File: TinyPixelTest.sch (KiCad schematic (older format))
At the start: 40 parts, among them IC1 ATTINY2313-S, P1 CONN_01X04, P2 CONN_01X04, P3 CONN_01X04, P4 CONN_01X04

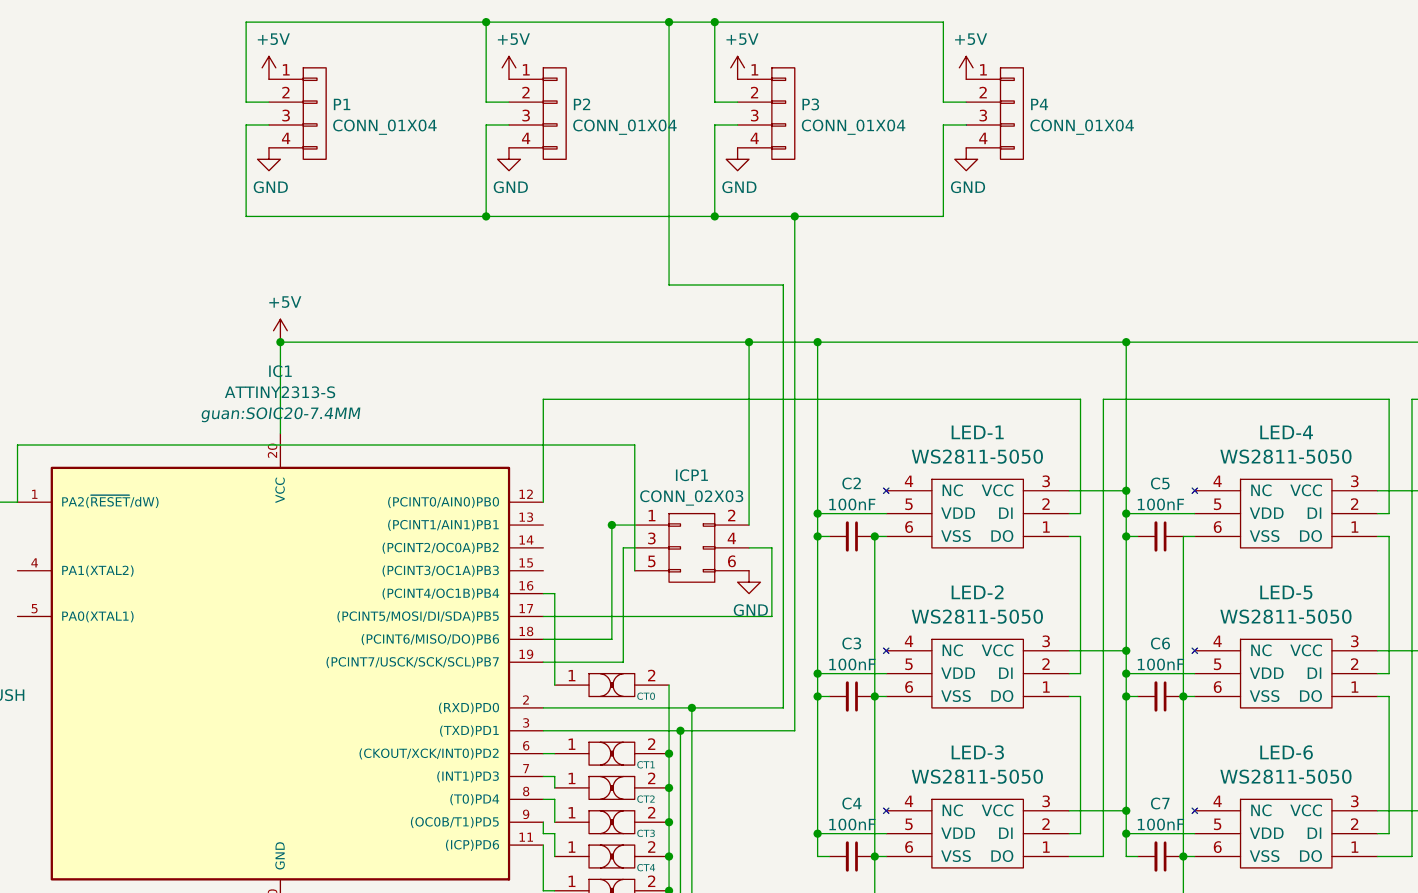
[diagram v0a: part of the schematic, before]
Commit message: Switched from 4 pin to 7 pin symmetrical connectors
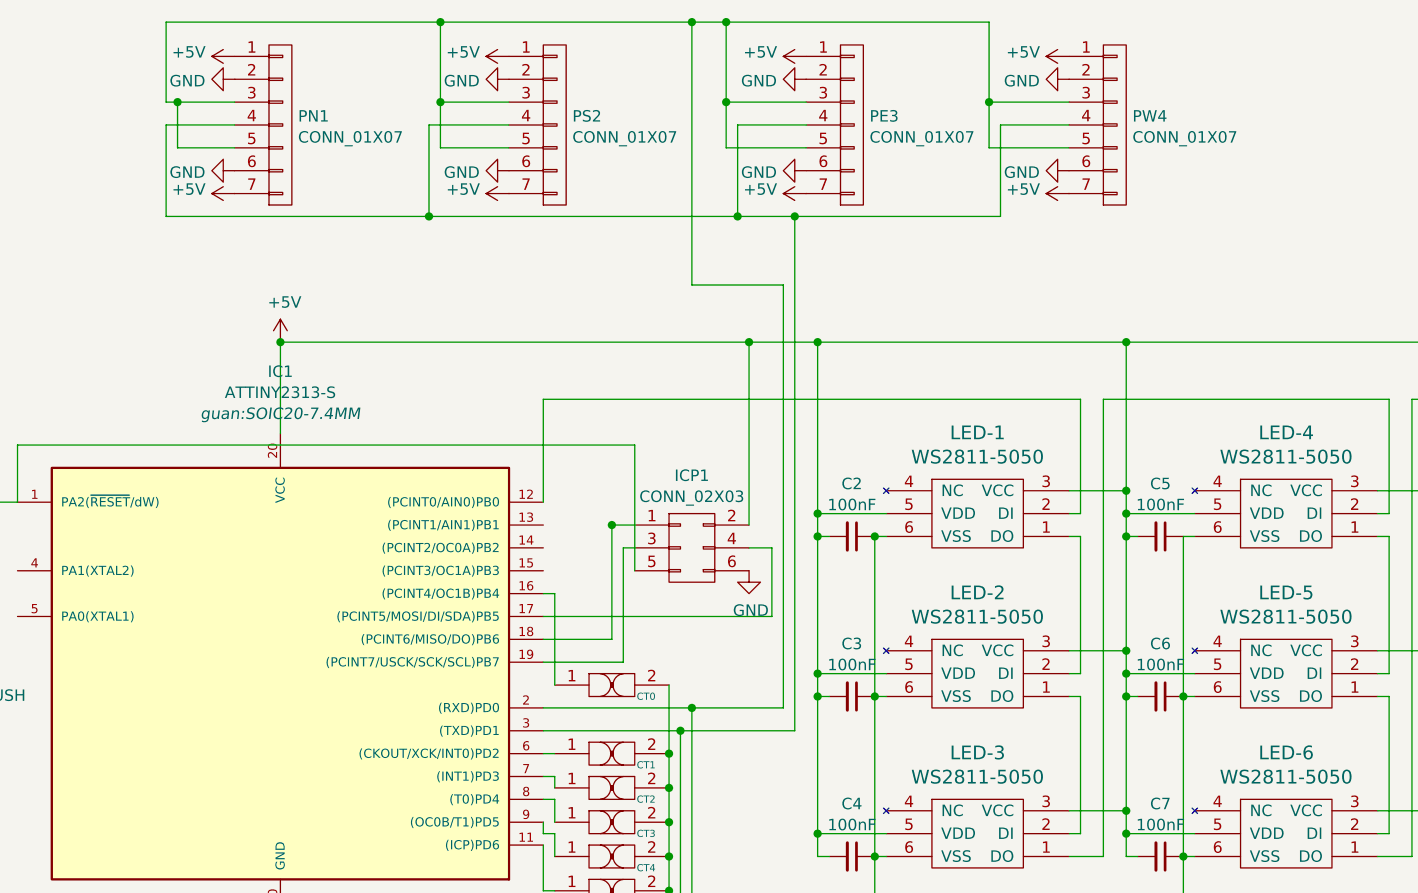
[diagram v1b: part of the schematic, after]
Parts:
- removed P1, P2, P3, P4: CONN_01X04, Pin_Headers:Pin_Header_Angled_1x04, symbol CONN_01X04
- added PE3, PN1: CONN_01X07, Pin_Headers:Pin_Header_Angled_1x07, symbol CONN_01X07
- added PS2, PW4: CONN_01X07, Socket_Strips:Socket_Strip_Angled_1x07, symbol CONN_01X07
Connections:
- net +5V: now also PE3.1 (P1), PE3.7 (P7), PN1.1 (P1), PN1.7 (P7), PS2.1 (P1), PS2.7 (P7), PW4.1 (P1), PW4.7 (P7)
- net GND: now also PE3.2 (P2), PE3.6 (P6), PN1.2 (P2), PN1.6 (P6), PS2.2 (P2), PS2.6 (P6), PW4.2 (P2), PW4.6 (P6)
- net at ESP1.2 (P2), IC1.2 ((RXD)PD0): now also PE3.3 (P3), PE3.5 (P5), PN1.3 (P3), PN1.5 (P5), PS2.3 (P3), PS2.5 (P5), PW4.3 (P3), PW4.5 (P5)
- net at ESP1.4 (P4), IC1.3 ((TXD)PD1): now also PE3.4 (P4), PN1.4 (P4), PS2.4 (P4), PW4.4 (P4)

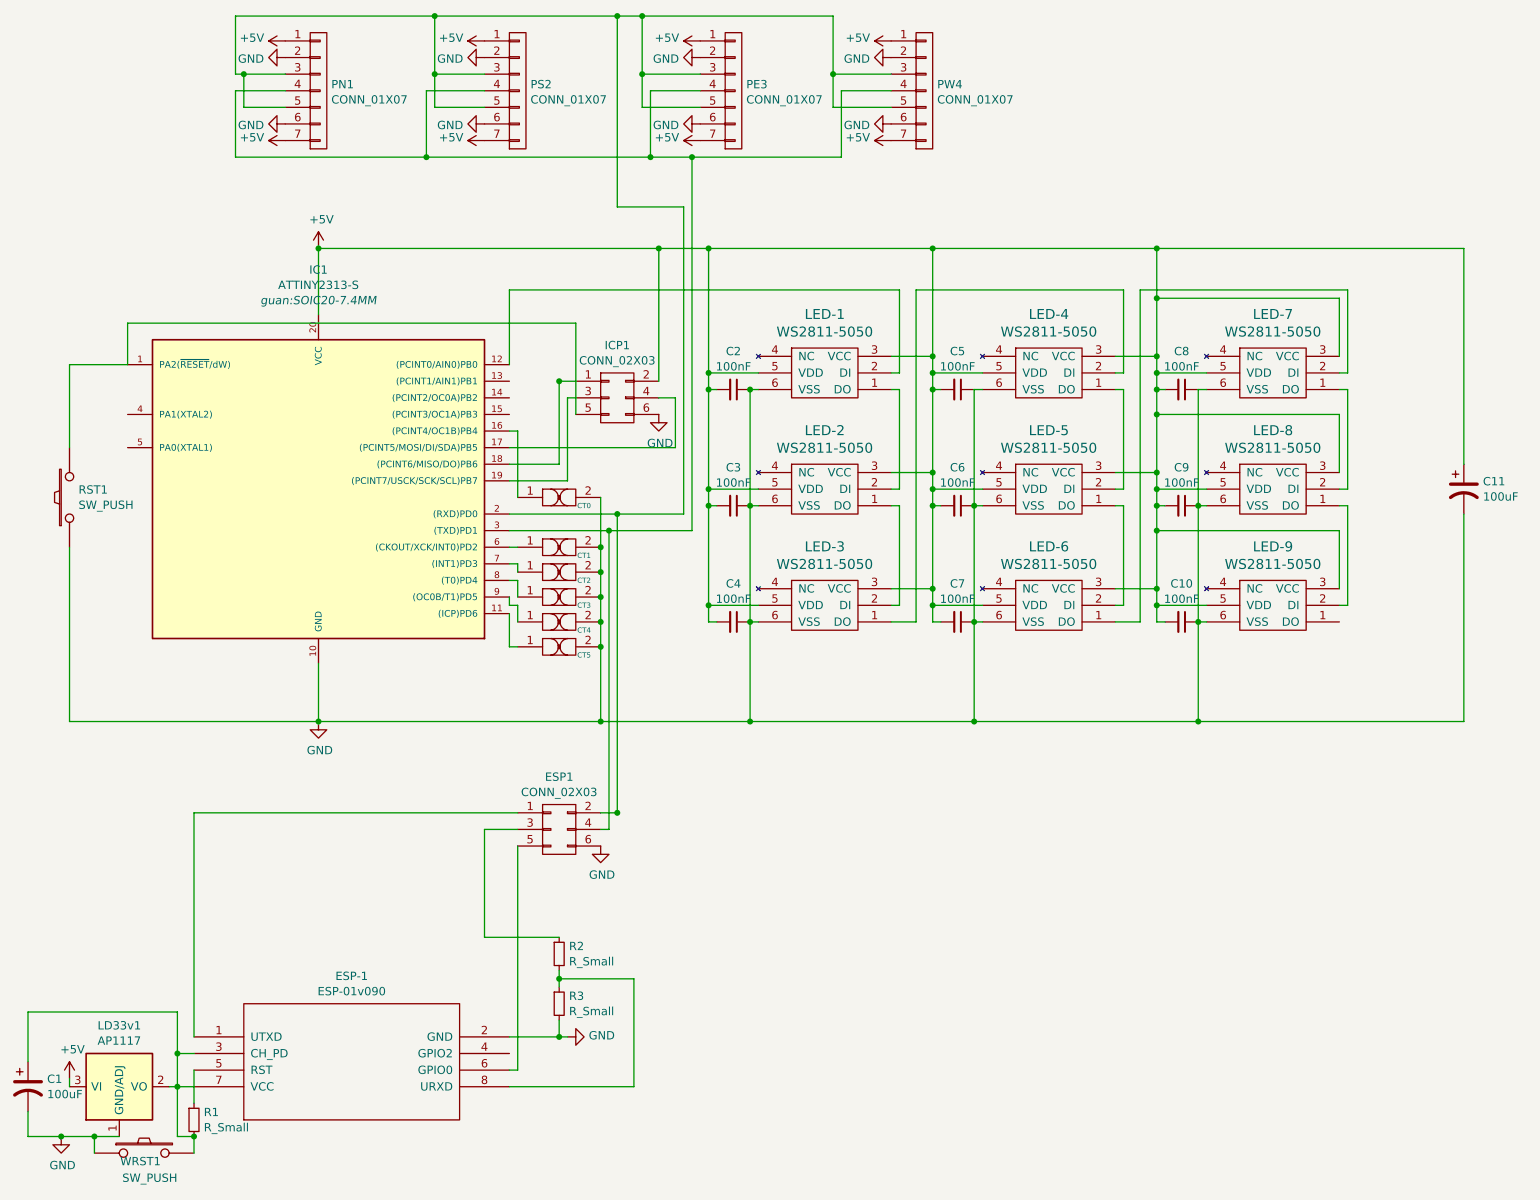
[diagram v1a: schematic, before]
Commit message: Fixed wire position
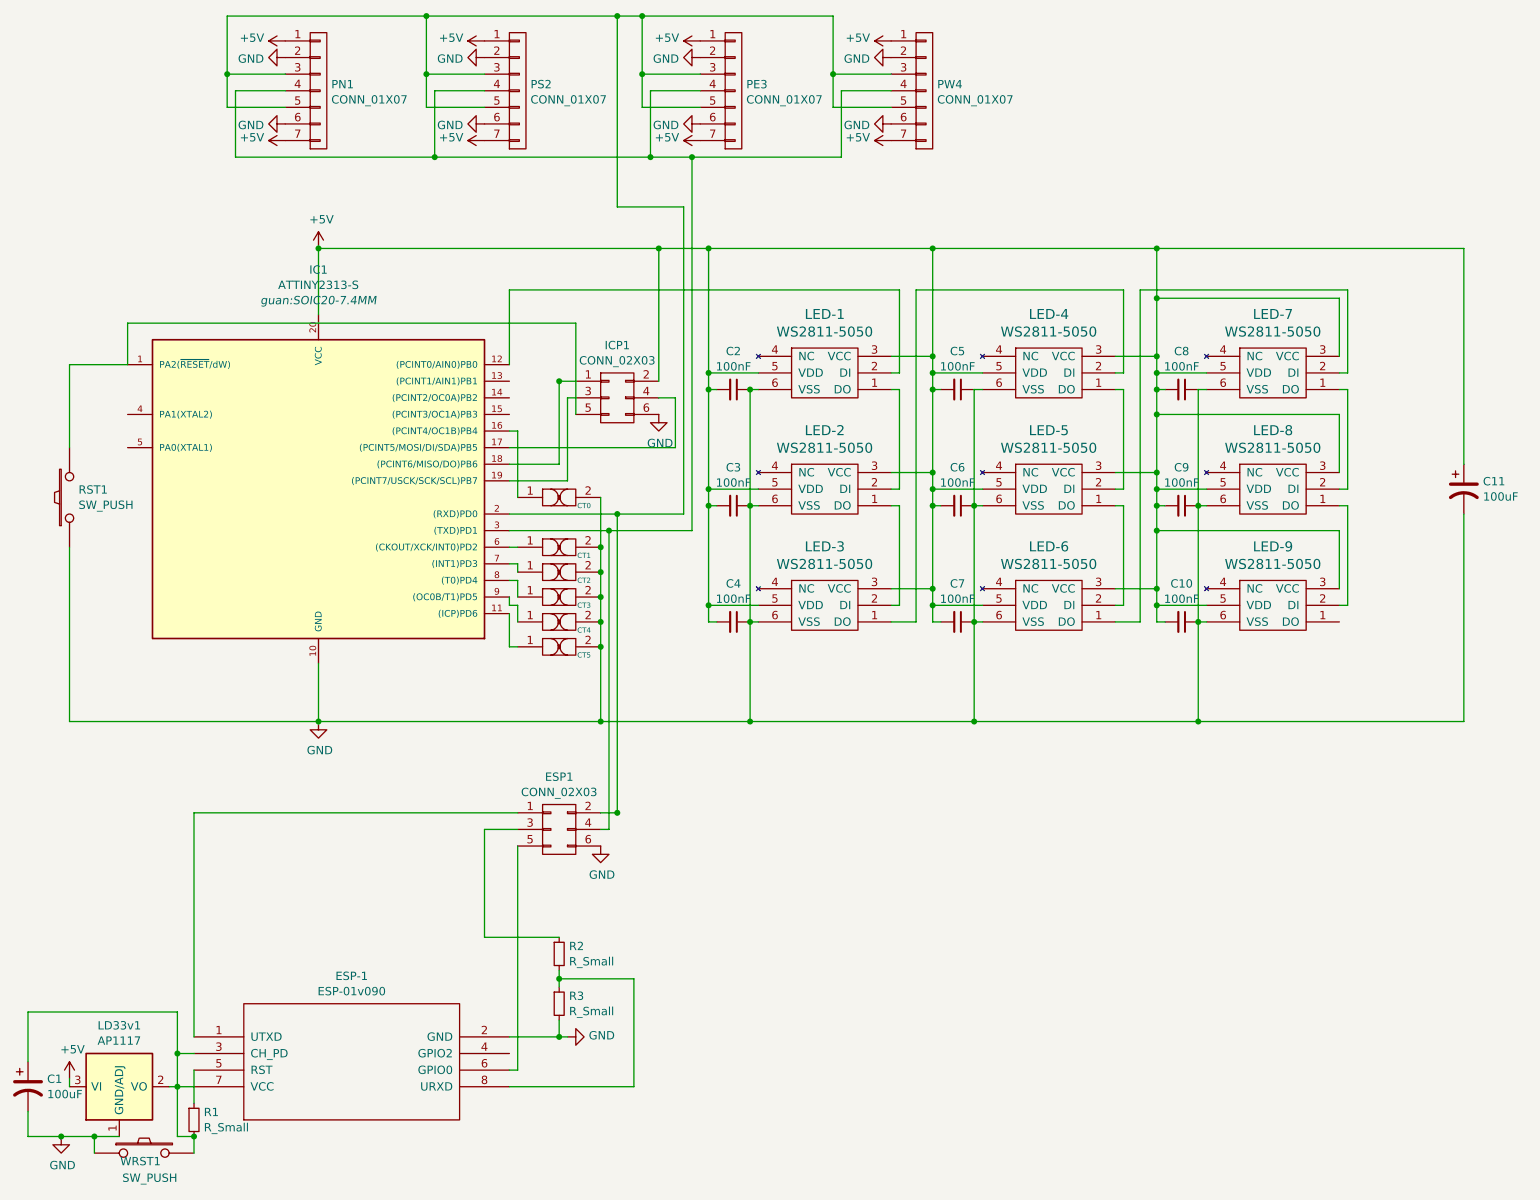
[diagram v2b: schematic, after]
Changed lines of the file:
@@
 $EndComp
 Wire Wire Line
-	4750 1950 4750 4200
+	4750 1950 4750 2700
+Wire Wire Line
+	4750 2700 4750 2800
+Wire Wire Line
+	4750 2800 4750 3400
+Wire Wire Line
+	4750 3400 4750 3500
+Wire Wire Line
+	4750 3500 4750 4100
+Wire Wire Line
+	4750 4100 4750 4200
 Wire Wire Line
 	4750 4100 5050 4100
@@
 Connection ~ 4750 2700
 Wire Wire Line
-	6100 1950 6100 4200
+	6100 1950 6100 2600
+Wire Wire Line
+	6100 2600 6100 2700
+Wire Wire Line
+	6100 2700 6100 2800
+Wire Wire Line
+	6100 2800 6100 3300
+Wire Wire Line
+	6100 3300 6100 3400
+Wire Wire Line
+	6100 3400 6100 3500
+Wire Wire Line
+	6100 3500 6100 4000
+Wire Wire Line
+	6100 4000 6100 4100
+Wire Wire Line
+	6100 4100 6100 4200
 Wire Wire Line
 	6100 4100 6400 4100
@@
 Connection ~ 6100 3400
 Wire Wire Line
-	7450 1950 7450 4200
+	7450 1950 7450 2250
+Wire Wire Line
+	7450 2250 7450 2600
+Wire Wire Line
+	7450 2600 7450 2700
+Wire Wire Line
+	7450 2700 7450 2800
+Wire Wire Line
+	7450 2800 7450 2950
+Wire Wire Line
+	7450 2950 7450 3300
+Wire Wire Line
+	7450 3300 7450 3400
+Wire Wire Line
+	7450 3400 7450 3500
+Wire Wire Line
+	7450 3500 7450 3650
+Wire Wire Line
+	7450 3650 7450 4000
+Wire Wire Line
+	7450 4000 7450 4100
+Wire Wire Line
+	7450 4100 7450 4200
 Wire Wire Line
 	7450 4100 7750 4100
@@
 Connection ~ 7450 2700
 Wire Wire Line
-	2400 1950 9300 1950
+	2400 1950 4450 1950
+Wire Wire Line
+	4450 1950 4750 1950
+Wire Wire Line
+	4750 1950 6100 1950
+Wire Wire Line
+	6100 1950 7450 1950
+Wire Wire Line
+	7450 1950 9300 1950
 Connection ~ 6100 1950
 Wire Wire Line
 	5000 2800 5050 2800
 Wire Wire Line
-	5000 4800 5000 2800
+	5000 4800 5000 4200
+Wire Wire Line
+	5000 4200 5000 3500
+Wire Wire Line
+	5000 3500 5000 2800
 Wire Wire Line
 	5050 3500 5000 3500
@@
 Connection ~ 5000 4200
 Wire Wire Line
-	6350 4800 6350 2800
+	6350 4800 6350 4200
+Wire Wire Line
+	6350 4200 6350 3500
+Wire Wire Line
+	6350 3500 6350 2800
 Wire Wire Line
 	6350 2800 6400 2800
@@
 Connection ~ 6350 4200
 Wire Wire Line
-	7700 4800 7700 2800
+	7700 4800 7700 4200
+Wire Wire Line
+	7700 4200 7700 3500
+Wire Wire Line
+	7700 3500 7700 2800
 Wire Wire Line
 	7700 2800 7750 2800
@@
 Connection ~ 7700 4200
 Wire Wire Line
-	900  4800 9300 4800
+	900  4800 2400 4800
+Wire Wire Line
+	2400 4800 4100 4800
+Wire Wire Line
+	4100 4800 5000 4800
+Wire Wire Line
+	5000 4800 6350 4800
+Wire Wire Line
+	6350 4800 7700 4800
+Wire Wire Line
+	7700 4800 9300 4800
 Connection ~ 6350 4800
 Wire Wire Line
@@
 	900  7000 900  6950
 Wire Wire Line
-	3550 6700 3900 6700
+	3550 6700 3850 6700
+Wire Wire Line
+	3850 6700 3900 6700
 Wire Wire Line
 	1650 5350 1650 6700
 Wire Wire Line
-	3550 3550 4600 3550
-Wire Wire Line
-	650  7300 1200 7300
+	3550 3550 4200 3550
+Wire Wire Line
+	4200 3550 4600 3550
+Wire Wire Line
+	650  7300 850  7300
+Wire Wire Line
+	850  7300 1050 7300
+Wire Wire Line
+	1050 7300 1200 7300
 Wire Wire Line
 	1650 5350 3600 5350
@@
 Connection ~ 3850 6700
 Wire Wire Line
-	3850 6300 3850 6400
+	3850 6300 3850 6350
+Wire Wire Line
+	3850 6350 3850 6400
 Wire Wire Line
 	3850 6350 4300 6350
@@
 Connection ~ 850  7300
 Wire Wire Line
-	1500 7000 1650 7000
+	1500 7000 1550 7000
+Wire Wire Line
+	1550 7000 1650 7000
 Connection ~ 1650 7300
 Wire Wire Line
@@
 	1550 7300 1650 7300
 Wire Wire Line
-	1550 6550 1550 7300
+	1550 6550 1550 6800
+Wire Wire Line
+	1550 6800 1550 7000
+Wire Wire Line
+	1550 7000 1550 7300
 Connection ~ 1550 7000
 Wire Wire Line
@@
 $EndComp
 Wire Wire Line
-	3550 3650 4650 3650
+	3550 3650 4150 3650
+Wire Wire Line
+	4150 3650 4650 3650
 $Comp
 L CUT-1 CT2
@@
 	3550 4350 3600 4350
 Wire Wire Line
-	4100 3450 4100 4800
+	4100 3450 4100 3750
+Wire Wire Line
+	4100 3750 4100 3900
+Wire Wire Line
+	4100 3900 4100 4050
+Wire Wire Line
+	4100 4050 4100 4200
+Wire Wire Line
+	4100 4200 4100 4350
+Wire Wire Line
+	4100 4350 4100 4800
 Connection ~ 4100 4800
 Connection ~ 4100 4350
@@
 	4700 900  4350 900
 Wire Wire Line
-	4350 550  4350 1100
-Wire Wire Line
-	1900 550  5500 550
-Wire Wire Line
-	1900 550  1900 900
-Wire Wire Line
-	1900 900  2200 900
-Wire Wire Line
-	3100 550  3100 1100
-Wire Wire Line
-	3100 900  3400 900
-Connection ~ 3100 550
-Wire Wire Line
-	5500 550  5500 1100
+	4350 550  4350 900
+Wire Wire Line
+	4350 900  4350 1100
+Wire Wire Line
+	1850 550  3050 550
+Wire Wire Line
+	3050 550  4200 550
+Wire Wire Line
+	4200 550  4350 550
+Wire Wire Line
+	4350 550  5500 550
+Wire Wire Line
+	1850 550  1850 900
+Wire Wire Line
+	1850 900  1850 900
+Wire Wire Line
+	1850 900  2200 900
+Wire Wire Line
+	3050 550  3050 900
+Wire Wire Line
+	3050 900  3050 1100
+Wire Wire Line
+	3050 900  3400 900
+Connection ~ 3050 550
+Wire Wire Line
+	5500 550  5500 900
+Wire Wire Line
+	5500 900  5500 1100
 Wire Wire Line
 	5500 900  5850 900
@@
 	5550 1000 5550 1400
 Wire Wire Line
-	5550 1400 1900 1400
+	5550 1400 4650 1400
+Wire Wire Line
+	4650 1400 4400 1400
+Wire Wire Line
+	4400 1400 3100 1400
+Wire Wire Line
+	3100 1400 1900 1400
 Wire Wire Line
 	1900 1400 1900 1000
@@
 	1900 1000 2200 1000
 Wire Wire Line
-	3400 1000 3050 1000
-Wire Wire Line
-	3050 1000 3050 1400
-Connection ~ 3050 1400
+	3400 1000 3100 1000
+Wire Wire Line
+	3100 1000 3100 1400
+Connection ~ 3100 1400
 Wire Wire Line
 	4700 1000 4400 1000
@@
 $EndComp
 Wire Wire Line
-	1950 900  1950 1100
-Wire Wire Line
-	1950 1100 2200 1100
-Connection ~ 1950 900
+	1850 900  1850 1100
+Wire Wire Line
+	1850 1100 2200 1100
+Connection ~ 1850 900
 $Comp
 L CONN_01X07 PS2
@@
 Connection ~ 4350 900
 Wire Wire Line
-	3100 1100 3400 1100
-Connection ~ 3100 900
+	3050 1100 3400 1100
+Connection ~ 3050 900
 $Comp
 L GND #PWR012

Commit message: Uhhh
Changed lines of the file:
@@
 Connection ~ 4150 3650
 Wire Wire Line
-	4600 3550 4600 1700
-Wire Wire Line
-	4600 1700 4200 1700
+	4600 1450 4600 3550
+Wire Wire Line
+	1850 1450 4600 1450
 Connection ~ 4200 3550
 $Comp
@@
 	1850 550  3050 550
 Wire Wire Line
-	3050 550  4200 550
-Wire Wire Line
-	4200 550  4350 550
+	3050 550  4350 550
 Wire Wire Line
 	4350 550  5500 550
@@
 	1850 550  1850 900
 Wire Wire Line
-	1850 900  1850 900
+	1850 900  1850 1100
+Wire Wire Line
+	1850 1100 1850 1450
 Wire Wire Line
 	1850 900  2200 900
@@
 	5850 1000 5550 1000
 Wire Wire Line
-	5550 1000 5550 1400
-Wire Wire Line
-	5550 1400 4650 1400
-Wire Wire Line
-	4650 1400 4400 1400
-Wire Wire Line
-	4400 1400 3100 1400
-Wire Wire Line
-	3100 1400 1900 1400
+	5550 1400 5550 1000
+Wire Wire Line
+	1900 1400 3100 1400
+Wire Wire Line
+	3100 1400 4400 1400
+Wire Wire Line
+	4400 1400 4650 1400
+Wire Wire Line
+	4650 1400 5550 1400
 Wire Wire Line
 	1900 1400 1900 1000
@@
 	4400 1000 4400 1400
 Connection ~ 4400 1400
-Wire Wire Line
-	4200 1700 4200 550
-Connection ~ 4200 550
 Connection ~ 4650 1400
 $Comp
@@
 $EndComp
 Wire Wire Line
-	1850 900  1850 1100
-Wire Wire Line
 	1850 1100 2200 1100
 Connection ~ 1850 900
@@
 	0    1    1    0
 $EndComp
+Connection ~ 1850 1100
 $EndSCHEMATC
